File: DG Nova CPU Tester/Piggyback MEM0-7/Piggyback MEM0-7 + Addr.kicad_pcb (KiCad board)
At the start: 4 copper layers, 73.9 x 53.5 mm, 26 parts, among them J1 Conn_02x18_Odd_Even, J2 Arduino Digital Pins, J3 Conn_01x17, J4 Arduino Digital Pins, J5 Conn_01x08, J6 Conn_01x08, SW1 Arduino Mega Reset, SW2 SW_DIP_x04, U1 74LS03, U2 74LS03, U3 74LS04, U4 74HC595, U5 74LS03, U6 74LS03, U7 74LS03, U8 74LS03, U9 74HC595

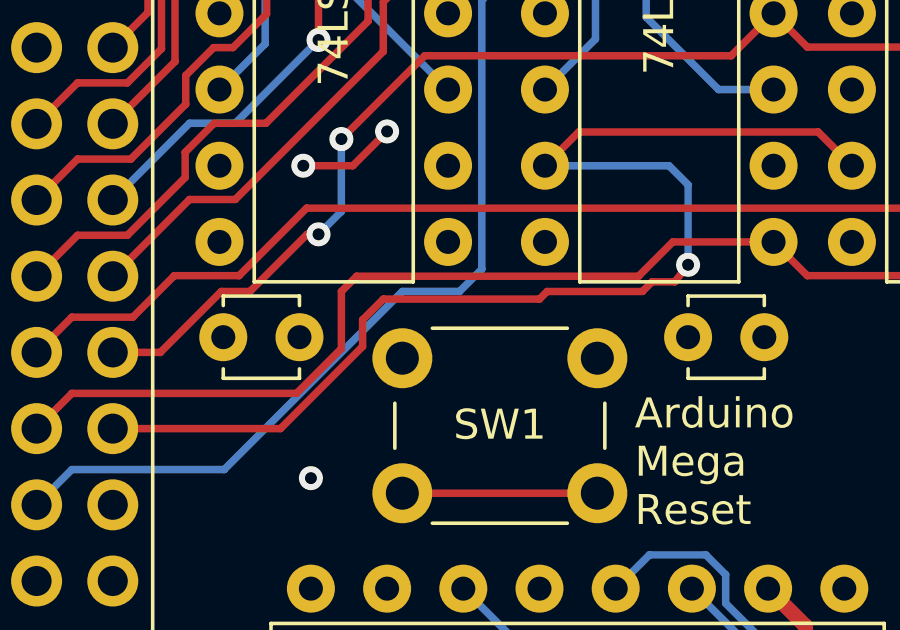
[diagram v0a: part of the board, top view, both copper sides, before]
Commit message: Fix reset button polarity
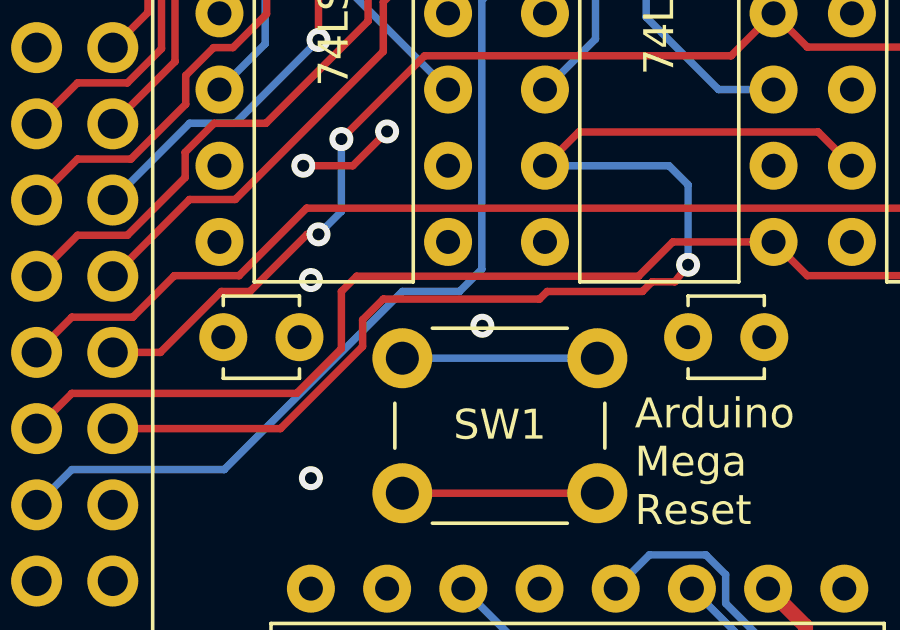
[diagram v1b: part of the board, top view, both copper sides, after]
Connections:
- SW1 pad 1: GND -> RST1
- SW1 pad 2: RST1 -> GND
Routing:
- net GND: track 3.72 -> 13.3 mm, vias 0 -> 2
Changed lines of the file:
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@@
       (stroke (width 0.1) (type solid)) (fill none) (layer "F.Fab"))
     (pad "1" thru_hole circle (at 0 0 90) (size 2 2) (drill 1.1) (layers "*.Cu" "*.Mask")
-      (net 2 "GND") (pinfunction "1") (pintype "passive"))
+      (net 63 "RST1") (pinfunction "1") (pintype "passive"))
     (pad "1" thru_hole circle (at 6.5 0 90) (size 2 2) (drill 1.1) (layers "*.Cu" "*.Mask")
-      (net 2 "GND") (pinfunction "1") (pintype "passive"))
+      (net 63 "RST1") (pinfunction "1") (pintype "passive"))
     (pad "2" thru_hole circle (at 0 4.5 90) (size 2 2) (drill 1.1) (layers "*.Cu" "*.Mask")
-      (net 63 "RST1") (pinfunction "2") (pintype "passive"))
+      (net 2 "GND") (pinfunction "2") (pintype "passive"))
     (pad "2" thru_hole circle (at 6.5 4.5 90) (size 2 2) (drill 1.1) (layers "*.Cu" "*.Mask")
-      (net 63 "RST1") (pinfunction "2") (pintype "passive"))
+      (net 2 "GND") (pinfunction "2") (pintype "passive"))
     (model "${KICAD6_3DMODEL_DIR}/Button_Switch_THT.3dshapes/SW_PUSH_6mm.wrl"
       (offset (xyz 0 0 0))
@@
   (segment (start 83.185 71.628) (end 83.344 71.469) (width 0.25) (layer "B.Cu") (net 1))
   (segment (start 83.312 65.659) (end 83.459 65.806) (width 0.4) (layer "B.Cu") (net 1))
-  (segment (start 80.96 90.043) (end 81.661 90.744) (width 0.5) (layer "In2.Cu") (net 2))
-  (segment (start 80.645 90.043) (end 80.96 90.043) (width 0.5) (layer "In2.Cu") (net 2))
-  (segment (start 78.232 90.043) (end 80.645 90.043) (width 0.5) (layer "In2.Cu") (net 2))
+  (segment (start 81.661 95.244) (end 88.161 95.244) (width 0.25) (layer "F.Cu") (net 2))
+  (via (at 84.328 89.662) (size 0.8) (drill 0.4) (layers "F.Cu" "B.Cu") (net 2))
+  (via (at 78.613 88.138) (size 0.8) (drill 0.4) (layers "F.Cu" "B.Cu") (net 2))
+  (segment (start 84.328 89.662) (end 84.328 89.789) (width 0.25) (layer "In1.Cu") (net 2))
+  (segment (start 84.582 89.789) (end 84.328 89.662) (width 0.25) (layer "In1.Cu") (net 2))
+  (segment (start 83.349679 89.154) (end 82.333679 88.138) (width 1) (layer "In2.Cu") (net 2))
+  (segment (start 84.328 89.662) (end 83.82 89.154) (width 1) (layer "In2.Cu") (net 2))
+  (segment (start 83.82 89.154) (end 83.349679 89.154) (width 1) (layer "In2.Cu") (net 2))
+  (segment (start 82.333679 88.138) (end 78.613 88.138) (width 1) (layer "In2.Cu") (net 2))
   (segment (start 136.144 77.724) (end 136.144 70.485) (width 0.25) (layer "F.Cu") (net 8))
   (segment (start 73.184 79.216) (end 72.009 80.391) (width 0.25) (layer "F.Cu") (net 8))
@@
   (segment (start 131.808 111.107) (end 132.461 111.76) (width 0.25) (layer "B.Cu") (net 61))
   (segment (start 130.683 89.662) (end 131.808 90.787) (width 0.25) (layer "B.Cu") (net 61))
-  (segment (start 81.661 95.244) (end 88.161 95.244) (width 0.25) (layer "F.Cu") (net 63))
+  (segment (start 81.661 90.744) (end 88.161 90.744) (width 0.25) (layer "B.Cu") (net 63))
   (segment (start 108.458 95.758) (end 100.076 95.758) (width 0.25) (layer "In2.Cu") (net 64))
   (segment (start 86.415 79.248) (end 84.836 80.827) (width 0.25) (layer "In2.Cu") (net 64))
